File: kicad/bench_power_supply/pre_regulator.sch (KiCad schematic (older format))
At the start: 0 parts

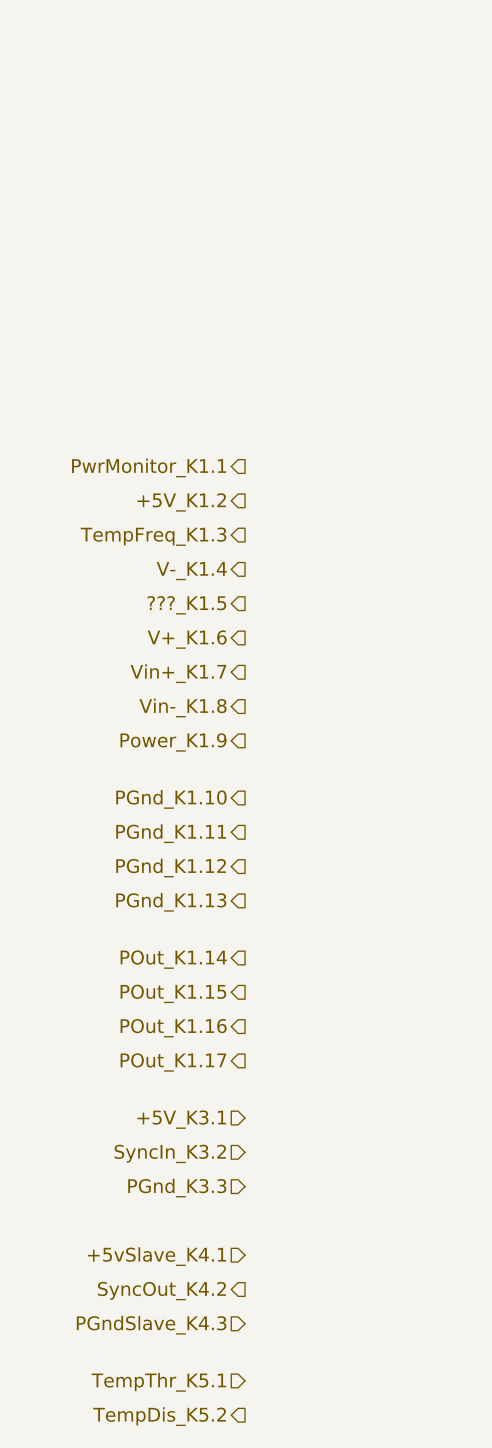
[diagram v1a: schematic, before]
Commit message: Added hlabels to pre-regulator
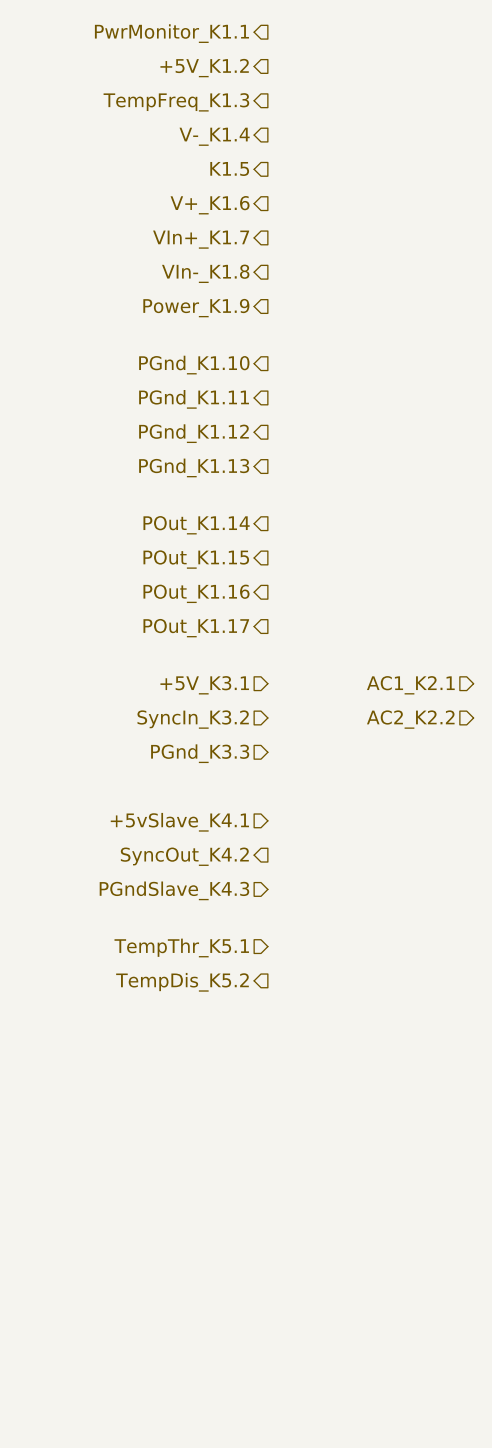
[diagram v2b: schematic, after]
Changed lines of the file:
@@
 Comment4 ""
 $EndDescr
-Text HLabel 1350 6000 0    60   Input ~ 0
+Text HLabel 1450 4100 0    60   Input ~ 0
 +5V_K3.1
-Text HLabel 1350 6150 0    60   Input ~ 0
+Text HLabel 1450 4250 0    60   Input ~ 0
 SyncIn_K3.2
-Text HLabel 1350 6300 0    60   Input ~ 0
+Text HLabel 1450 4400 0    60   Input ~ 0
 PGnd_K3.3
-Text HLabel 1350 7150 0    60   Input ~ 0
+Text HLabel 1450 5250 0    60   Input ~ 0
 TempThr_K5.1
-Text HLabel 1350 7300 0    60   Output ~ 0
+Text HLabel 1450 5400 0    60   Output ~ 0
 TempDis_K5.2
-Text HLabel 1350 3300 0    60   Output ~ 0
+Text HLabel 1450 1400 0    60   Output ~ 0
 +5V_K1.2
-Text HLabel 1350 3150 0    60   Output ~ 0
+Text HLabel 1450 1250 0    60   Output ~ 0
 PwrMonitor_K1.1
-Text HLabel 1350 3450 0    60   Output ~ 0
+Text HLabel 1450 1550 0    60   Output ~ 0
 TempFreq_K1.3
-Text HLabel 1350 5450 0    60   Output ~ 0
+Text HLabel 1450 3550 0    60   Output ~ 0
 POut_K1.15
-Text HLabel 1350 5300 0    60   Output ~ 0
+Text HLabel 1450 3400 0    60   Output ~ 0
 POut_K1.14
-Text HLabel 1350 5750 0    60   Output ~ 0
+Text HLabel 1450 3850 0    60   Output ~ 0
 POut_K1.17
-Text HLabel 1350 5600 0    60   Output ~ 0
+Text HLabel 1450 3700 0    60   Output ~ 0
 POut_K1.16
-Text HLabel 1350 4750 0    60   Output ~ 0
+Text HLabel 1450 2850 0    60   Output ~ 0
 PGnd_K1.11
-Text HLabel 1350 4600 0    60   Output ~ 0
+Text HLabel 1450 2700 0    60   Output ~ 0
 PGnd_K1.10
-Text HLabel 1350 5050 0    60   Output ~ 0
+Text HLabel 1450 3150 0    60   Output ~ 0
 PGnd_K1.13
-Text HLabel 1350 4900 0    60   Output ~ 0
+Text HLabel 1450 3000 0    60   Output ~ 0
 PGnd_K1.12
-Text HLabel 1350 4350 0    60   Output ~ 0
+Text HLabel 1450 2450 0    60   Output ~ 0
 Power_K1.9
-Text HLabel 1350 3600 0    60   Output ~ 0
+Text HLabel 1450 1700 0    60   Output ~ 0
 V-_K1.4
-Text HLabel 1350 3900 0    60   Output ~ 0
+Text HLabel 1450 2000 0    60   Output ~ 0
 V+_K1.6
-Text HLabel 1350 3750 0    60   Output ~ 0
-???_K1.5
-Text HLabel 1350 4050 0    60   Output ~ 0
-Vin+_K1.7
-Text HLabel 1350 4200 0    60   Output ~ 0
-Vin-_K1.8
-Text HLabel 1350 6600 0    60   Input ~ 0
+Text HLabel 1450 1850 0    60   Output ~ 0
+K1.5
+Text HLabel 1450 2150 0    60   Output ~ 0
+VIn+_K1.7
+Text HLabel 1450 2300 0    60   Output ~ 0
+VIn-_K1.8
+Text HLabel 1450 4700 0    60   Input ~ 0
 +5vSlave_K4.1
-Text HLabel 1350 6750 0    60   Output ~ 0
+Text HLabel 1450 4850 0    60   Output ~ 0
 SyncOut_K4.2
-Text HLabel 1350 6900 0    60   Input ~ 0
+Text HLabel 1450 5000 0    60   Input ~ 0
 PGndSlave_K4.3
+Text HLabel 2350 4100 0    60   Input ~ 0
+AC1_K2.1
+Text HLabel 2350 4250 0    60   Input ~ 0
+AC2_K2.2
 $EndSCHEMATC

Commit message: Updated pre_regulator
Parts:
- added B1: D_BRIDGE, ~, symbol D_BRIDGE
- added C1: 1uF, symbol C_SMALL
- added C2: 10000uF, symbol CP1_SMALL
- added C?: 560pF, symbol C_SMALL
- added C?: 470uF, symbol C_SMALL
- added D1, D2, D3: D_SMALL, symbol D_SMALL
- added D? (x2): ZENERSMALL, symbol ZENERSMALL
- added K2: CONN_01X02, symbol CONN_01X02
- added Q? (x2): IRF5210PBF, TO-220AB, symbol IRF5210PBF
- added Q? (x2): MMBT5401, SOT-23, symbol MMBT5401
- added Q?: SCR, symbol SCR
- added R5, R6, R? (x2): 100R, symbol R_SMALL
- added R? (x2): 18k, symbol R_SMALL
- added R?: 240k, symbol R_SMALL
- added R?: 82k, symbol R_SMALL
- added R?: 39k, symbol R_SMALL
- added R?: 3k3, symbol R_SMALL
- added R? (x2): 4k7, symbol R_SMALL
- added R?: 10k, symbol R_SMALL
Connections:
- net labels added: DcOut_K1.18, GND, PGND
- wire segments 0 -> 72

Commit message: Split pre-regulator into two new schemas. Previous pre_regulator.sch has been renamed to pre_regulator_module.
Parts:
- R4: renamed from R?; value 100R -> 1k5
- gave numbers to parts that had none: 19
- renumbered C2 to C4
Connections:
- net labels added: DcOut, PGnd, POut, PowerOnOff
- net labels removed: +5V_K1.2, +5V_K3.1, +5vSlave_K4.1, AC1_K2.1, AC2_K2.2, DcOut_K1.18, K1.5, PGndSlave_K4.3, PGnd_K1.10, PGnd_K1.11, PGnd_K1.12, PGnd_K1.13, PGnd_K3.3, POut_K1.14, POut_K1.15, POut_K1.16, POut_K1.17, Power_K1.9, PwrMonitor_K1.1, SyncIn_K3.2, SyncOut_K4.2, TempDis_K5.2, TempFreq_K1.3, TempThr_K5.1, V+_K1.6, V-_K1.4, VIn+_K1.7, VIn-_K1.8
- wire segments 72 -> 94
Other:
- moved on the sheet: K2, Q1, Q2, Q3, Q4, Q5

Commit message: added files from mint
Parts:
- removed K2: CONN_01X02, symbol CONN_01X02
- B1: symbol D_BRIDGE -> D_Bridge
- C1, C2, C3: symbol C_SMALL -> C_Small
- C4: symbol CP1_SMALL -> CP1_Small
- D1, D2, D3: symbol D_SMALL -> D_Small
- R1, R10, R11, R12, R13, R2, R3, R4, R5, R6, R7, R8, R9: symbol R_SMALL -> R_Small
- Z1, Z2: symbol ZENERSMALL -> ZENERsmall
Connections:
- net labels added: AC1, AC2
- wire segments 94 -> 60
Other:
- moved on the sheet: Q1, Q2, Q3, Q4, Q5

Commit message: commiting before install linux mint
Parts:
- added Q?: IRF5210PBF, TO-220AB, symbol IRF5210PBF
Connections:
- net POut: now also Q?.3 (S)
- net at B1.3 (+), D3.2 (A), Q1.2 (D)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: now also Q?.2 (D)
- net at Q2.1 (G), R6.1: now also Q?.1 (G)
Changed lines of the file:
@@
 Text HLabel 1150 2200 0    60   Input ~ 0
 AC2
+$Comp
+L IRF5210PBF Q?
+U 1 1 579692C0
+P 4975 1575
+F 0 "Q?" V 5160 1640 50  0000 L CNN
+F 1 "IRF5210PBF" V 5225 1275 25  0000 L CNN
+F 2 "TO-220AB" V 5175 1300 25  0000 L CIN
+F 3 "~" H 4975 1575 50  0000 L CNN
+	1    4975 1575
+	0    -1   -1   0
+$EndComp
 $EndSCHEMATC
